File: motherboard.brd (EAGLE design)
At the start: 177.1 x 75.9 mm, 187 parts, among them IC1 LM2576, IC10 TUSB2046B, IC12 LM50, IC13 LM50, IC2 74LS595D, IC3 74LS595D, IC4 IC_FT230X-SSOP-16, IC5 VN5772AK, IC6 VN5772AK, IC7 VN5772AK, IC8 VN5772AK, IC9 VN5772AK, U2 NCP4625, U3 ATMEGA168, Y1 16Mhz, Y2 6MHz

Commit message: moved ruler
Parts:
- moved U$17 0.32 mm to (0.00, 75.9)
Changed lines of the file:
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@@
 <?xml version="1.0" encoding="utf-8"?>
 <!DOCTYPE eagle SYSTEM "eagle.dtd">
-<eagle version="6.5.0">
+<eagle version="6.1">
 <drawing>
 <settings>
@@
 </class>
 </classes>
-<designrules name="default">
+<designrules>
 <description language="de">&lt;b&gt;EAGLE Design Rules&lt;/b&gt;
 &lt;p&gt;
@@
 <element name="D5" library="adafruit" package="SOD-123" value="" x="143.51" y="15.24" rot="R180"/>
 <element name="SW1" library="alcoswitch" package="FSMSM" value="" x="-37.465" y="46.355"/>
-<element name="U$17" library="CAD Ruler_EagleCad Gridrunner XL Metric V1 (Rupert Hirst 2011)" package="RULER" value="" x="0" y="76.2"/>
+<element name="U$17" library="CAD Ruler_EagleCad Gridrunner XL Metric V1 (Rupert Hirst 2011)" package="RULER" value="" x="0" y="75.8825"/>
 <element name="U$18" library="CAD Ruler_EagleCad Gridrunner XL Metric V1 (Rupert Hirst 2011)" package="RULER" value="" x="0" y="0" rot="R90"/>
 <element name="C43" library="adafruit" package="C1206" value="0.1uF" x="30.48" y="7.62"/>

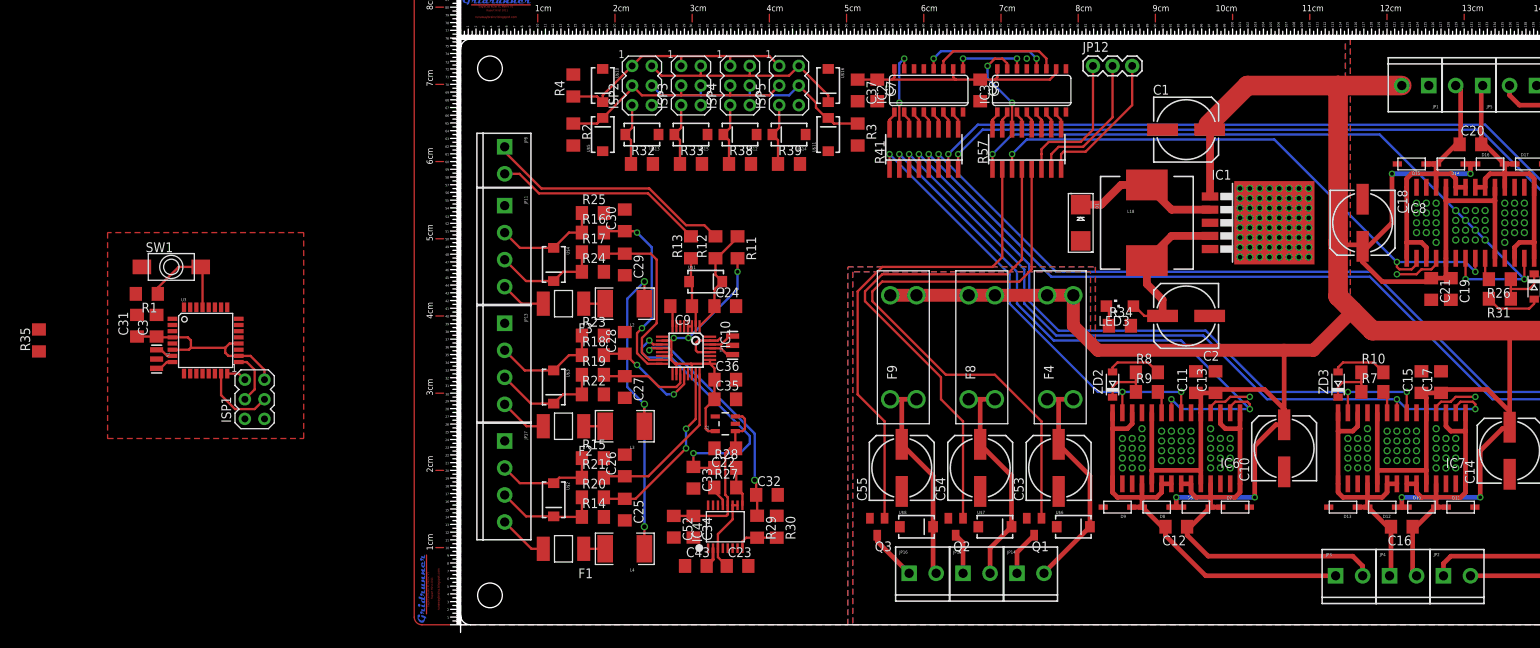
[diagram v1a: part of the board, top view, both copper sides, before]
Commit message: laying out mcu
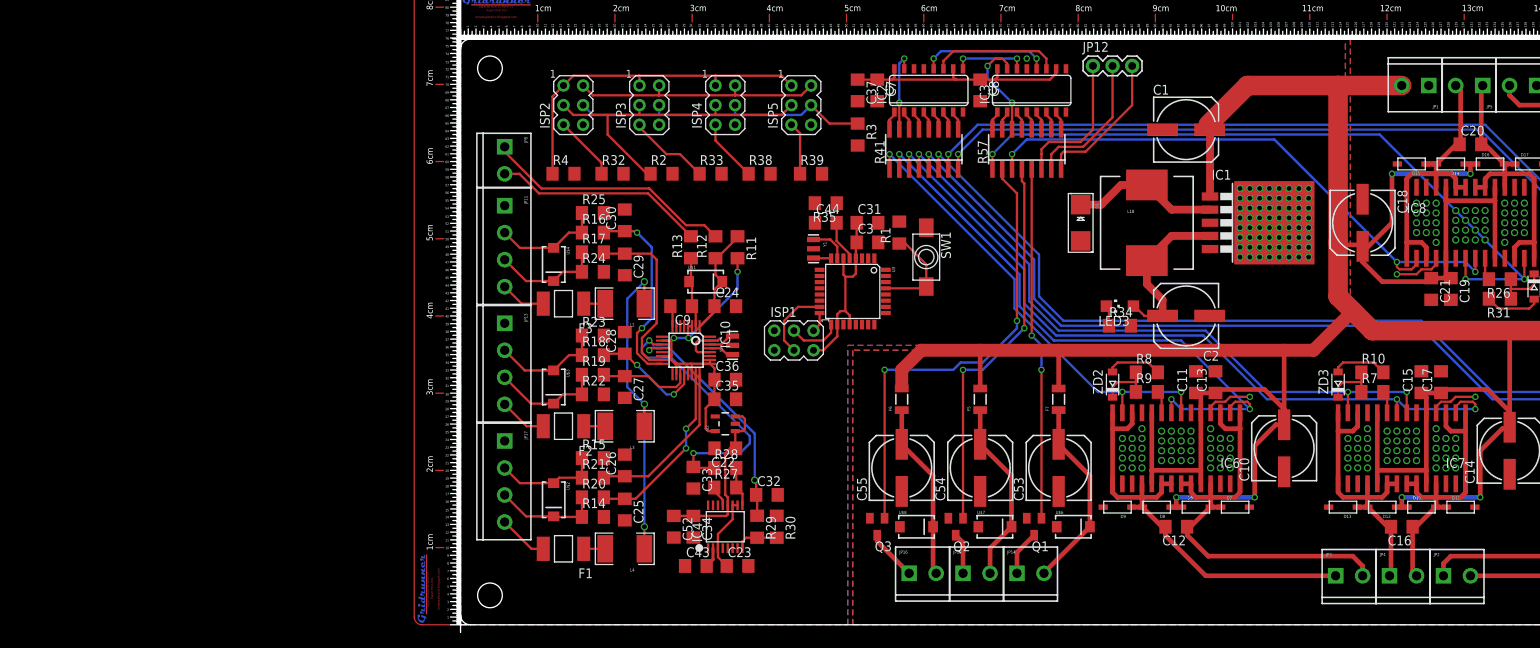
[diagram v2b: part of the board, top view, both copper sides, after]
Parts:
- removed F4, F8, F9: 3557-2, rov_club:3557-2
- removed U$10, U$11, U$12, U$13, U$14, U$15, U$16, U$5: TVS, sparkfun:SMA-DIODE
- added C44: 0.1uF, adafruit:C1206
- added F5, F6, F7: PTCSMD, sparkfun:PTC-1206
- moved R35 103.5 mm to (47.3, 54.6), turned to 180 degrees
- moved SW1 97.8 mm to (60.3, 47.6), turned to 270 degrees
- moved R1 97.8 mm to (56.8, 50.8), turned to 90 degrees
- moved C31 95.6 mm to (52.7, 52.1), turned to 0 degrees
- moved C3 92.7 mm to (52.7, 49.5), turned to 0 degrees
- moved Y1 86.3 mm to (45.7, 48.7)
- moved U3 84.1 mm to (50.8, 43.2), turned to 270 degrees
- moved ISP1 70.3 mm to (43.2, 36.8), turned to 270 degrees
- moved R2 12.5 mm to (26.0, 58.4), turned to 0 degrees
- moved R4 11.5 mm to (13.3, 58.4), turned to 0 degrees
- moved ISP2 9.25 mm to (14.6, 67.3)
- moved ISP3 5.97 mm to (24.4, 67.3)
- moved R32 4.02 mm to (19.7, 58.4)
- moved ISP4 3.17 mm to (34.3, 67.3)
- moved R39 3.13 mm to (45.4, 58.4)
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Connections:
- net +12V: now also F5.2, F6.2, F7.2; no longer F4.P$3, F4.P$4, F8.P$3, F8.P$4, F9.P$3, F9.P$4
- net +5V: now also C44.1; no longer U$16.C
- net AGND: now also C44.2
- net GND: no longer U$10.A, U$11.A, U$12.A, U$13.A, U$14.A, U$15.A, U$16.A, U$5.A
- net MISO: no longer U$10.C
- net MOSI: no longer U$11.C
- net N$50: now also F6.1; no longer F9.P$1, F9.P$2
- net N$51: no longer U$13.C
- net N$52: no longer U$15.C
- net N$53: no longer U$12.C
- net N$54: now also F5.1; no longer F8.P$1, F8.P$2
- net N$55: now also F7.1; no longer F4.P$1, F4.P$2
- net N$58: no longer U$14.C
- net SCK: no longer U$5.C
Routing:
- net SW2: track 77.0 -> 45.7 mm, vias 0 -> 2
- net SW1: track 68.4 -> 50.1 mm, vias 0 -> 2
- net MISO: track 33.0 -> 45.1 mm
- net SCK: track 49.1 -> 59.9 mm
- net MOSI: track 32.7 -> 40.1 mm
- net +12V: track 592.5 -> 599.1 mm
- net AGND: track 74.8 -> 80.1 mm
- net N$55: track 30.1 -> 25.3 mm
- net N$54: track 28.8 -> 24.0 mm
- net N$50: track 27.8 -> 23.0 mm
- net +5V: track 207.5 -> 211.8 mm
- net 2HB: track 110.0 -> 113.1 mm
- net 2HA: track 122.0 -> 124.9 mm
- net SW0: track 62.8 -> 60.0 mm, vias 0 -> 2
- net N$4: track 2.38 -> 4.98 mm
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
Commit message: still
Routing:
- net ISP-SCK: track 6.81 -> 60.3 mm, vias 0 -> 1
- net ISP-MISO: track 2.61 -> 42.0 mm, vias 0 -> 1
- net !EN4: track 0.00 -> 37.0 mm
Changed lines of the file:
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@@
 <wire x1="46.5074" y1="40.38" x2="46.5074" y2="38.8874" width="0.3048" layer="1"/>
 <wire x1="46.5074" y1="38.8874" x2="45.72" y2="38.1" width="0.3048" layer="1"/>
-<wire x1="14.757" y1="58.42" x2="46.5074" y2="40.38" width="0" layer="19" extent="1-1"/>
+<wire x1="14.757" y1="58.42" x2="16.51" y2="58.42" width="0.3048" layer="1"/>
+<via x="16.51" y="58.42" extent="1-16" drill="0.5"/>
+<wire x1="16.51" y1="58.42" x2="17.4625" y2="58.42" width="0.3048" layer="16"/>
+<wire x1="35.8775" y1="47.9425" x2="45.72" y2="38.1" width="0.3048" layer="16"/>
+<wire x1="17.4625" y1="58.42" x2="27.94" y2="47.9425" width="0.3048" layer="16"/>
+<wire x1="27.94" y1="47.9425" x2="35.8775" y2="47.9425" width="0.3048" layer="16"/>
 </signal>
 <signal name="ISP-SCK">
@@
 <wire x1="48" y1="37.84" x2="46.99" y2="36.83" width="0.3048" layer="1"/>
 <wire x1="46.99" y1="36.83" x2="44.45" y2="36.83" width="0.3048" layer="1"/>
-<wire x1="43.18" y1="38.1" x2="27.457" y2="58.42" width="0" layer="19" extent="1-1"/>
+<wire x1="27.457" y1="58.42" x2="29.21" y2="58.42" width="0.3048" layer="1"/>
+<via x="29.21" y="58.42" extent="1-16" drill="0.5"/>
+<wire x1="43.18" y1="38.1" x2="43.18" y2="39.6875" width="0.3048" layer="16"/>
+<wire x1="43.18" y1="39.6875" x2="35.56" y2="47.3075" width="0.3048" layer="16"/>
+<wire x1="35.56" y1="47.3075" x2="27.6225" y2="47.3075" width="0.3048" layer="16"/>
+<wire x1="27.6225" y1="47.3075" x2="17.4625" y2="57.4675" width="0.3048" layer="16"/>
+<wire x1="17.4625" y1="57.4675" x2="16.1925" y2="57.4675" width="0.3048" layer="16"/>
+<wire x1="16.1925" y1="57.4675" x2="15.5575" y2="58.1025" width="0.3048" layer="16"/>
+<wire x1="15.5575" y1="58.1025" x2="15.5575" y2="58.7375" width="0.3048" layer="16"/>
+<wire x1="15.5575" y1="58.7375" x2="16.1925" y2="59.3725" width="0.3048" layer="16"/>
+<wire x1="16.1925" y1="59.3725" x2="28.2575" y2="59.3725" width="0.3048" layer="16"/>
+<wire x1="28.2575" y1="59.3725" x2="29.21" y2="58.42" width="0.3048" layer="16"/>
 </signal>
 <signal name="ISP-MOSI">
@@
 <contactref element="JP8" pad="1"/>
 <wire x1="5.715" y1="61.9125" x2="5.715" y2="61.2775" width="0.3048" layer="1"/>
-<wire x1="5.715" y1="61.2775" x2="10.4775" y2="56.515" width="0.3048" layer="1"/>
-<wire x1="10.4775" y1="56.515" x2="24.4475" y2="56.515" width="0.3048" layer="1"/>
-<wire x1="24.4475" y1="56.515" x2="29.21" y2="51.7525" width="0.3048" layer="1"/>
+<wire x1="5.715" y1="61.2775" x2="10.795" y2="56.1975" width="0.3048" layer="1"/>
+<wire x1="10.795" y1="56.1975" x2="24.765" y2="56.1975" width="0.3048" layer="1"/>
+<wire x1="24.765" y1="56.1975" x2="29.21" y2="51.7525" width="0.3048" layer="1"/>
 <wire x1="29.21" y1="51.7525" x2="31.5845" y2="51.7525" width="0.3048" layer="1"/>
 <wire x1="31.5845" y1="51.7525" x2="33.02" y2="50.317" width="0.3048" layer="1"/>
@@
 <contactref element="JP8" pad="2"/>
 <wire x1="5.715" y1="58.4125" x2="7.6275" y2="58.4125" width="0.3048" layer="1"/>
-<wire x1="7.6275" y1="58.4125" x2="10.16" y2="55.88" width="0.3048" layer="1"/>
-<wire x1="10.16" y1="55.88" x2="24.282" y2="55.88" width="0.3048" layer="1"/>
-<wire x1="24.282" y1="55.88" x2="29.845" y2="50.317" width="0.3048" layer="1"/>
+<wire x1="7.6275" y1="58.4125" x2="10.4775" y2="55.5625" width="0.3048" layer="1"/>
+<wire x1="10.4775" y1="55.5625" x2="24.5995" y2="55.5625" width="0.3048" layer="1"/>
+<wire x1="24.5995" y1="55.5625" x2="29.845" y2="50.317" width="0.3048" layer="1"/>
 </signal>
 <signal name="AGND">
@@
 <contactref element="U3" pad="13"/>
 <contactref element="R32" pad="2"/>
-<wire x1="21.107" y1="58.42" x2="46.5074" y2="42.78" width="0" layer="19" extent="1-1"/>
+<wire x1="21.107" y1="58.42" x2="21.107" y2="57.633" width="0.3048" layer="1"/>
+<wire x1="21.107" y1="57.633" x2="21.9075" y2="56.8325" width="0.3048" layer="1"/>
+<wire x1="21.9075" y1="56.8325" x2="25.0825" y2="56.8325" width="0.3048" layer="1"/>
+<wire x1="25.0825" y1="56.8325" x2="29.5275" y2="52.3875" width="0.3048" layer="1"/>
+<wire x1="29.5275" y1="52.3875" x2="36.5125" y2="52.3875" width="0.3048" layer="1"/>
+<wire x1="36.5125" y1="52.3875" x2="37.465" y2="51.435" width="0.3048" layer="1"/>
+<wire x1="37.465" y1="51.435" x2="37.465" y2="43.4975" width="0.3048" layer="1"/>
+<wire x1="37.465" y1="43.4975" x2="38.1825" y2="42.78" width="0.3048" layer="1"/>
+<wire x1="46.5074" y1="42.78" x2="38.1825" y2="42.78" width="0.3048" layer="1"/>
 </signal>
 <signal name="!EN3">

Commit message: ...
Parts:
- moved C44 3.82 mm to (50.2, 54.6), turned to 180 degrees
- moved R35 2.54 mm to (47.3, 52.1)
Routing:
- net !RST: track 12.8 -> 78.6 mm, vias 0 -> 2
- net LATCH: track 16.8 -> 68.7 mm, vias 2 -> 3
- net RXD: track 0.00 -> 51.6 mm, vias 0 -> 2
- net TXD: track 0.00 -> 49.8 mm, vias 0 -> 2
- net ISP-MOSI: track 9.68 -> 51.1 mm, vias 0 -> 1
- net SCK: track 59.9 -> 83.9 mm, vias 0 -> 1
- net !EN3: track 0.00 -> 23.0 mm
- net MOSI: track 40.1 -> 61.4 mm, vias 0 -> 2
- net !EN2: track 0.00 -> 19.3 mm
- net +5V: track 211.8 -> 222.7 mm
- net 4HB: track 92.7 -> 101.8 mm
- net AGND: track 80.1 -> 83.8 mm
- net !EN4: track 37.0 -> 35.3 mm

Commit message: ...
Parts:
- added JP10, JP7, JP9: (no value), sparkfun:1X02
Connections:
- net +12V: now also JP10.2, JP7.2, JP9.2
- net N$50: now also JP10.1
- net N$54: now also JP9.1
- net N$55: now also JP7.1
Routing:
- net 2STAT: track 6.40 -> 179.6 mm, vias 1 -> 4
- net TEMP1: track 2.35 -> 174.5 mm, vias 0 -> 2
- net AGND: track 83.8 -> 238.4 mm, vias 0 -> 10
- net 2SENSE: track 7.36 -> 152.0 mm, vias 0 -> 4
- net 1STAT: track 6.40 -> 148.8 mm, vias 1 -> 4
- net 1SENSE: track 7.14 -> 122.1 mm, vias 0 -> 2
- net 0STAT: track 6.40 -> 114.2 mm, vias 1 -> 2
- net 0SENSE: track 7.14 -> 46.0 mm, vias 0 -> 2
- net !EN1: track 0.00 -> 21.7 mm, vias 0 -> 2
- net +12V: track 599.1 -> 612.2 mm
- net N$55: track 25.3 -> 29.6 mm
- net N$54: track 24.0 -> 28.3 mm
- net N$50: track 23.0 -> 27.3 mm
- net GND: vias 275 -> 287
